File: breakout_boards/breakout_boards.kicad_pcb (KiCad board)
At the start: 2 copper layers, 183 x 45.5 mm, 41 parts, among them J1 Power, J10 NeoPixel, J11 E0-Stop, J12 Z-Stop, J13 EM0, J14 THE0, J15 BLTouch, J16 THB, J17 Extension2, J18 POWER_EXP, J19 ZM2, J2 XM, J20 BED, J21 HE0, J22 HE1, J23 THE1, J24 FAN1, J25 HE2, J26 THE2, J27 FAN2, J28 TFT, J29 EXP2, J3 5V_PSU, J30 EM1, J31 E1-Stop, J32 I2C, J33 EM2, J34 E2-Stop, J35 UART, J36 SPI, J37 Extension1, J4 EXP1, J5 FAN0, J6 YM, J7 X-Stop, J8 ZM1, J9 Y-Stop

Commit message: updated schematics and pcb
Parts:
- J1: value Power -> XM; footprint Connector_Phoenix_MSTB:PhoenixContact_MSTBA_2,5_2-G_1x02_P5.00mm_Horizontal -> Connector_JST:JST_EH_B4B-EH-A_1x04_P2.50mm_Vertical
- J10: value NeoPixel -> BLTouch; footprint Connector_Phoenix_MSTB:PhoenixContact_MSTBA_2,5_3-G_1x03_P5.00mm_Horizontal -> Connector_JST:JST_EH_B5B-EH-A_1x05_P2.50mm_Vertical
- J11: value E0-Stop -> FAN1; footprint Connector_JST:JST_EH_B3B-EH-A_1x03_P2.50mm_Vertical -> Connector_JST:JST_EH_B2B-EH-A_1x02_P2.50mm_Vertical
- J12: value Z-Stop -> HE1; footprint Connector_JST:JST_EH_B3B-EH-A_1x03_P2.50mm_Vertical -> Connector_JST:JST_EH_B2B-EH-A_1x02_P2.50mm_Vertical
- J13: value EM0 -> THE1; footprint Connector_JST:JST_EH_B4B-EH-A_1x04_P2.50mm_Vertical -> Connector_JST:JST_EH_B2B-EH-A_1x02_P2.50mm_Vertical
- J14: value THE0 -> ZM1; footprint Connector_JST:JST_EH_B2B-EH-A_1x02_P2.50mm_Vertical -> Connector_JST:JST_EH_B4B-EH-A_1x04_P2.50mm_Vertical
- J15: value BLTouch -> FAN2; footprint Connector_JST:JST_EH_B5B-EH-A_1x05_P2.50mm_Vertical -> Connector_JST:JST_EH_B2B-EH-A_1x02_P2.50mm_Vertical
- J16: value THB -> HE2
- J17: value Extension2 -> THE2; footprint Connector_IDC:IDC-Header_2x20_P2.54mm_Vertical -> Connector_JST:JST_EH_B2B-EH-A_1x02_P2.50mm_Vertical
- J18: value POWER_EXP -> ZM2; footprint Connector_Phoenix_MSTB:PhoenixContact_MSTBA_2,5_3-G_1x03_P5.00mm_Horizontal -> Connector_JST:JST_EH_B4B-EH-A_1x04_P2.50mm_Vertical
- J19: value ZM2 -> TFT; footprint Connector_JST:JST_EH_B4B-EH-A_1x04_P2.50mm_Vertical -> Connector_JST:JST_EH_B5B-EH-A_1x05_P2.50mm_Vertical
- J2: value XM -> NeoPixel; footprint Connector_JST:JST_EH_B4B-EH-A_1x04_P2.50mm_Vertical -> Connector_Phoenix_MSTB:PhoenixContact_MSTBA_2,5_3-G_1x03_P5.00mm_Horizontal
- J20: value BED -> EXP2; footprint Connector_JST:JST_EH_B2B-EH-A_1x02_P2.50mm_Vertical -> Connector_IDC:IDC-Header_2x05_P2.54mm_Vertical
- J21: value HE0 -> EM0; footprint Connector_JST:JST_EH_B2B-EH-A_1x02_P2.50mm_Vertical -> Connector_JST:JST_EH_B4B-EH-A_1x04_P2.50mm_Vertical
- J22: value HE1 -> E0-Stop; footprint Connector_JST:JST_EH_B2B-EH-A_1x02_P2.50mm_Vertical -> Connector_JST:JST_EH_B3B-EH-A_1x03_P2.50mm_Vertical
- J23: value THE1 -> X-Stop; footprint Connector_JST:JST_EH_B2B-EH-A_1x02_P2.50mm_Vertical -> Connector_JST:JST_EH_B3B-EH-A_1x03_P2.50mm_Vertical
- J24: value FAN1 -> EM1; footprint Connector_JST:JST_EH_B2B-EH-A_1x02_P2.50mm_Vertical -> Connector_JST:JST_EH_B4B-EH-A_1x04_P2.50mm_Vertical
- J25: value HE2 -> E1-Stop; footprint Connector_JST:JST_EH_B2B-EH-A_1x02_P2.50mm_Vertical -> Connector_JST:JST_EH_B3B-EH-A_1x03_P2.50mm_Vertical
- J26: value THE2 -> Y-Stop; footprint Connector_JST:JST_EH_B2B-EH-A_1x02_P2.50mm_Vertical -> Connector_JST:JST_EH_B3B-EH-A_1x03_P2.50mm_Vertical
- J27: value FAN2 -> I2C; footprint Connector_JST:JST_EH_B2B-EH-A_1x02_P2.50mm_Vertical -> Connector_JST:JST_EH_B4B-EH-A_1x04_P2.50mm_Vertical
- J28: value TFT -> EM2; footprint Connector_JST:JST_EH_B5B-EH-A_1x05_P2.50mm_Vertical -> Connector_JST:JST_EH_B4B-EH-A_1x04_P2.50mm_Vertical
- J29: value EXP2 -> E2-Stop; footprint Connector_IDC:IDC-Header_2x05_P2.54mm_Vertical -> Connector_JST:JST_EH_B3B-EH-A_1x03_P2.50mm_Vertical
- J3: value 5V_PSU -> BED; footprint Connector_Phoenix_MSTB:PhoenixContact_MSTBA_2,5_2-G_1x02_P5.00mm_Horizontal -> Connector_JST:JST_EH_B2B-EH-A_1x02_P2.50mm_Vertical
- J30: value EM1 -> Z-Stop; footprint Connector_JST:JST_EH_B4B-EH-A_1x04_P2.50mm_Vertical -> Connector_JST:JST_EH_B3B-EH-A_1x03_P2.50mm_Vertical
- J31: value E1-Stop -> Power; footprint Connector_JST:JST_EH_B3B-EH-A_1x03_P2.50mm_Vertical -> Connector_Phoenix_MSTB:PhoenixContact_MSTBA_2,5_2-G_1x02_P5.00mm_Horizontal
- J32: value I2C -> 5V_PSU; footprint Connector_JST:JST_EH_B4B-EH-A_1x04_P2.50mm_Vertical -> Connector_Phoenix_MSTB:PhoenixContact_MSTBA_2,5_2-G_1x02_P5.00mm_Horizontal
- J33: value EM2 -> UART
- J34: value E2-Stop -> POWER_EXP; footprint Connector_JST:JST_EH_B3B-EH-A_1x03_P2.50mm_Vertical -> Connector_Phoenix_MSTB:PhoenixContact_MSTBA_2,5_3-G_1x03_P5.00mm_Horizontal
- J35: value UART -> SPI; footprint Connector_JST:JST_EH_B4B-EH-A_1x04_P2.50mm_Vertical -> Connector_JST:JST_EH_B6B-EH-A_1x06_P2.50mm_Vertical
- J36: value SPI -> Extension1; footprint Connector_JST:JST_EH_B6B-EH-A_1x06_P2.50mm_Vertical -> Connector_IDC:IDC-Header_2x20_P2.54mm_Vertical
- J37: value Extension1 -> Extension2
- J4: value EXP1 -> THB; footprint Connector_IDC:IDC-Header_2x05_P2.54mm_Vertical -> Connector_JST:JST_EH_B2B-EH-A_1x02_P2.50mm_Vertical
- J6: value YM -> EXP1; footprint Connector_JST:JST_EH_B4B-EH-A_1x04_P2.50mm_Vertical -> Connector_IDC:IDC-Header_2x05_P2.54mm_Vertical
- J7: value X-Stop -> YM; footprint Connector_JST:JST_EH_B3B-EH-A_1x03_P2.50mm_Vertical -> Connector_JST:JST_EH_B4B-EH-A_1x04_P2.50mm_Vertical
- J8: value ZM1 -> HE0; footprint Connector_JST:JST_EH_B4B-EH-A_1x04_P2.50mm_Vertical -> Connector_JST:JST_EH_B2B-EH-A_1x02_P2.50mm_Vertical
- J9: value Y-Stop -> THE0; footprint Connector_JST:JST_EH_B3B-EH-A_1x03_P2.50mm_Vertical -> Connector_JST:JST_EH_B2B-EH-A_1x02_P2.50mm_Vertical
- moved H1 179.6 mm to (57.8, 70.0), turned to 0 degrees
- moved J28 137.9 mm to (72.8, 97.2)
- moved J36 137.5 mm to (60.0, 108.0), turned to 90 degrees
- moved J2 120.5 mm to (222.8, 101.2)
- moved J24 119.8 mm to (58.8, 97.2)
- moved H3 106.1 mm to (196.8, 70.8), turned to 0 degrees
- moved J22 92.7 mm to (99.8, 70.5)
- moved J29 91.0 mm to (122.8, 70.5), turned to 0 degrees
- moved J25 90.5 mm to (111.2, 70.5)
- moved J23 90.3 mm to (65.2, 70.5)
- moved J26 88.0 mm to (76.8, 70.5)
- moved J21 82.6 mm to (100.8, 97.2)
- moved J35 74.2 mm to (153.2, 84.0), turned to 0 degrees
- moved J31 65.6 mm to (211.0, 77.0), turned to 180 degrees
- moved J4 62.5 mm to (127.8, 84.0), turned to 0 degrees
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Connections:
- J1 pad 1: GND -> XM_4
- J1 pad 2: VCC -> XM_3
- J10 pad 1: +5V -> GND
- J10 pad 2: NeoPixel -> +5V
- J10 pad 3: GND -> BLT_PWM
- J11 pad 1: E0-STOP -> FAN1
- J11 pad 2: GND -> VCC
- J12 pad 1: Z-STOP -> VCC
- J12 pad 2: GND -> HE1
- J13 pad 1: EM0_4 -> THE1
- J13 pad 2: EM0_3 -> GND
- J14 pad 1: THE0 -> ZM1_4
- J14 pad 2: GND -> ZM1_3
- J15 pad 1: GND -> FAN2
- J15 pad 2: +5V -> VCC
- J16 pad 1: THB -> VCC
- J16 pad 2: GND -> HE2
- J17 pad 1: EXP1_1 -> THE2
- J17 pad 2: BLT_PWM -> GND
- J18 pad 1: GND -> ZM2_4
- J18 pad 2: VCC -> ZM2_3
- J18 pad 3: +5V -> ZM2_2
- J19 pad 1: ZM2_4 -> +5V
- J19 pad 2: ZM2_3 -> GND
- J19 pad 3: ZM2_2 -> TX1
- J19 pad 4: ZM2_1 -> RX1
- J2 pad 1: XM_4 -> +5V
- J2 pad 2: XM_3 -> NeoPixel
- J2 pad 3: XM_2 -> GND
- J20 pad 1: VCC -> EXP2_1
- J20 pad 2: BED -> EXP2_2
- J21 pad 1: VCC -> EM0_4
- J21 pad 2: HE0 -> EM0_3
- J22 pad 1: VCC -> E0-STOP
- J22 pad 2: HE1 -> GND
- J23 pad 1: THE1 -> X-STOP
- J24 pad 1: FAN1 -> EM1_4
- J24 pad 2: VCC -> EM1_3
- J25 pad 1: VCC -> E1-STOP
- J25 pad 2: HE2 -> GND
- J26 pad 1: THE2 -> Y-STOP
- J27 pad 1: FAN2 -> +5V
- J27 pad 2: VCC -> GND
- J28 pad 1: +5V -> EM2_4
- J28 pad 2: GND -> EM2_3
- J28 pad 3: TX1 -> EM2_2
- J28 pad 4: RX1 -> EM2_1
- J29 pad 1: EXP2_1 -> E2-STOP
- J29 pad 2: EXP2_2 -> GND
- J29 pad 3: EXP2_3 -> +3V3
- J3 pad 1: GND -> VCC
- J3 pad 2: +5V -> BED
- J30 pad 1: EM1_4 -> Z-STOP
- J30 pad 2: EM1_3 -> GND
- J30 pad 3: EM1_2 -> +3V3
- J31 pad 1: E1-STOP -> GND
- J31 pad 2: GND -> VCC
- J32 pad 1: +5V -> GND
- J32 pad 2: GND -> +5V
- J33 pad 1: EM2_4 -> +5V
- J33 pad 2: EM2_3 -> GND
- J33 pad 3: EM2_2 -> TX3
- J33 pad 4: EM2_1 -> RX3
- J34 pad 1: E2-STOP -> GND
- J34 pad 2: GND -> VCC
- J34 pad 3: +3V3 -> +5V
- J35 pad 3: TX3 -> MOSI
- J35 pad 4: RX3 -> MISO
- J36 pad 1: +5V -> EM1_4
- J36 pad 2: GND -> XM_4
- J36 pad 3: MOSI -> EM1_3
- J36 pad 4: MISO -> XM_3
- J36 pad 5: CS -> EM1_2
- J36 pad 6: SCK -> XM_2
- J37 pad 1: EM1_4 -> EXP1_1
- J37 pad 10: YM_4 -> THB
- J37 pad 11: EM2_3 -> EXP1_6
- J37 pad 12: YM_3 -> THE1
- J37 pad 13: EM2_2 -> EXP1_7
- J37 pad 14: YM_2 -> THE2
- J37 pad 15: EM2_1 -> EXP1_8
- J37 pad 16: YM_1 -> FAN0
- J37 pad 17: X-STOP -> EXP2_1
- J37 pad 18: ZM1_4 -> FAN1
- J37 pad 19: Y-STOP -> EXP2_2
- J37 pad 2: XM_4 -> BLT_TRIGGER
- J37 pad 20: ZM1_3 -> FAN2
- J37 pad 21: Z-STOP -> EXP2_3
- J37 pad 22: ZM1_2 -> GND
- J37 pad 23: E0-STOP -> EXP2_4
- J37 pad 24: ZM1_1 -> GND
- J37 pad 25: E1-STOP -> EXP2_5
- J37 pad 26: ZM2_4 -> SCL
- J37 pad 27: E2-STOP -> EXP2_6
- J37 pad 28: ZM2_3 -> SDA
- J37 pad 29: THB -> EXP2_7
- J37 pad 3: EM1_3 -> EXP1_2
- J37 pad 30: ZM2_2 -> MOSI
- J37 pad 31: THE0 -> EXP2_10
- J37 pad 32: ZM2_1 -> MISO
- J37 pad 33: THE1 -> TX1
- J37 pad 34: EM0_4 -> CS
- J37 pad 35: THE2 -> RX1
- J37 pad 36: EM0_3 -> SCK
- J37 pad 37: GND -> RST
- J37 pad 38: EM0_2 -> TX3
- J37 pad 39: +3V3 -> GND
- J37 pad 4: XM_3 -> BLT_PWM
- J37 pad 40: EM0_1 -> RX3
- J37 pad 5: EM1_2 -> EXP1_3
- J37 pad 6: XM_2 -> NeoPixel
- J37 pad 7: EM1_1 -> EXP1_4
- J37 pad 8: XM_1 -> THE0
- J37 pad 9: EM2_4 -> EXP1_5
- J4 pad 1: EXP1_1 -> THB
- J4 pad 2: EXP1_2 -> GND
- J6 pad 1: YM_4 -> EXP1_1
- J6 pad 2: YM_3 -> EXP1_2
- J6 pad 3: YM_2 -> EXP1_3
- J6 pad 4: YM_1 -> EXP1_4
- J7 pad 1: X-STOP -> YM_4
- J7 pad 2: GND -> YM_3
- J7 pad 3: +3V3 -> YM_2
- J8 pad 1: ZM1_4 -> VCC
- J8 pad 2: ZM1_3 -> HE0
- J9 pad 1: Y-STOP -> THE0
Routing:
- net GND: track 410.0 -> 548.0 mm, vias 3 -> 0
- net +5V: track 304.1 -> 206.8 mm, vias 3 -> 0
- net BED: track 21.0 -> 71.6 mm
- net HE0: track 19.0 -> 57.3 mm
- net SDA: track 11.2 -> 40.0 mm, vias 0 -> 1
- net SCL: track 11.6 -> 39.7 mm, vias 0 -> 1
- net EXP1_1: track 41.6 -> 65.3 mm
- net E2-STOP: track 38.6 -> 60.8 mm
- net EXP1_2: track 43.3 -> 64.2 mm
- net EXP1_5: track 37.2 -> 56.2 mm
- net SCK: track 9.99 -> 29.0 mm
- net EXP2_2: track 43.6 -> 61.6 mm
- net HE1: track 22.6 -> 40.4 mm
- net THE2: track 28.1 -> 10.5 mm, vias 0 -> 1
- net EXP2_3: track 40.2 -> 56.7 mm
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
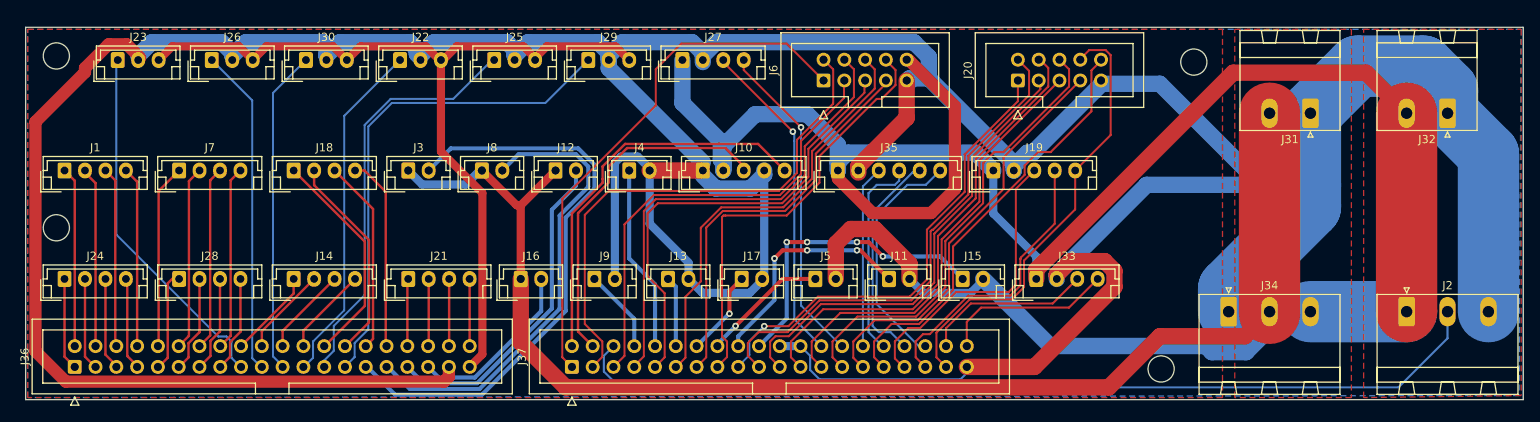
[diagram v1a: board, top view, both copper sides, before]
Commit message: changed mounting hole footprint and connector jst eh to jst xh
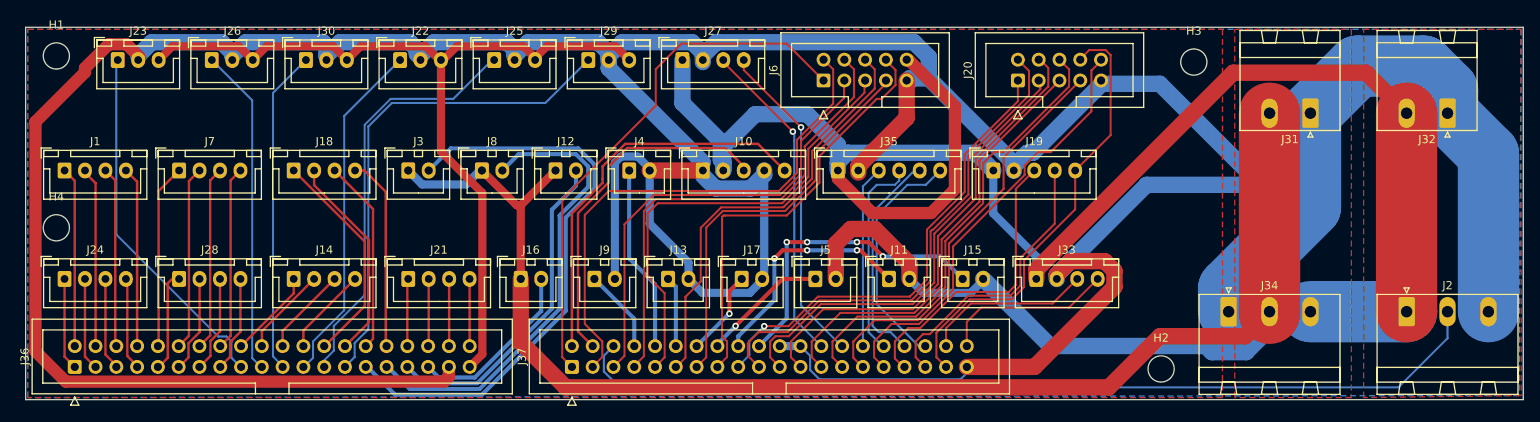
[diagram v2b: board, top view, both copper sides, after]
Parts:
- H1, H2, H3, H4: footprint MountingHole:MountingHole_3.2mm_M3 -> MountingHole:MountingHole_3.2mm_M3_DIN965
- J1, J14, J18, J21, J24, J27, J28, J33, J7: footprint Connector_JST:JST_EH_B4B-EH-A_1x04_P2.50mm_Vertical -> Connector_JST:JST_XH_B4B-XH-A_1x04_P2.50mm_Vertical
- J10, J19: footprint Connector_JST:JST_EH_B5B-EH-A_1x05_P2.50mm_Vertical -> Connector_JST:JST_XH_B5B-XH-A_1x05_P2.50mm_Vertical
- J11, J12, J13, J15, J16, J17, J3, J4, J5, J8, J9: footprint Connector_JST:JST_EH_B2B-EH-A_1x02_P2.50mm_Vertical -> Connector_JST:JST_XH_B2B-XH-A_1x02_P2.50mm_Vertical
- J22, J23, J25, J26, J29, J30: footprint Connector_JST:JST_EH_B3B-EH-A_1x03_P2.50mm_Vertical -> Connector_JST:JST_XH_B3B-XH-A_1x03_P2.50mm_Vertical
- J35: footprint Connector_JST:JST_EH_B6B-EH-A_1x06_P2.50mm_Vertical -> Connector_JST:JST_XH_B6B-XH-A_1x06_P2.50mm_Vertical
